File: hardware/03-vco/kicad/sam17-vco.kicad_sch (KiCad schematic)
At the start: 32 parts, among them J1 PSU +12/G/G/-12, J2 Mazo digital IDC 2x6, U10 74HC14, U11 L78L05, U12 LD1117S33TR, U13 TMP1075DGK, U14 24AA02E48, U5 AD5686RBRUZ, U6 AD5686RBRUZ, U7 AD5686RBRUZ, U8 ADR4525BRZ

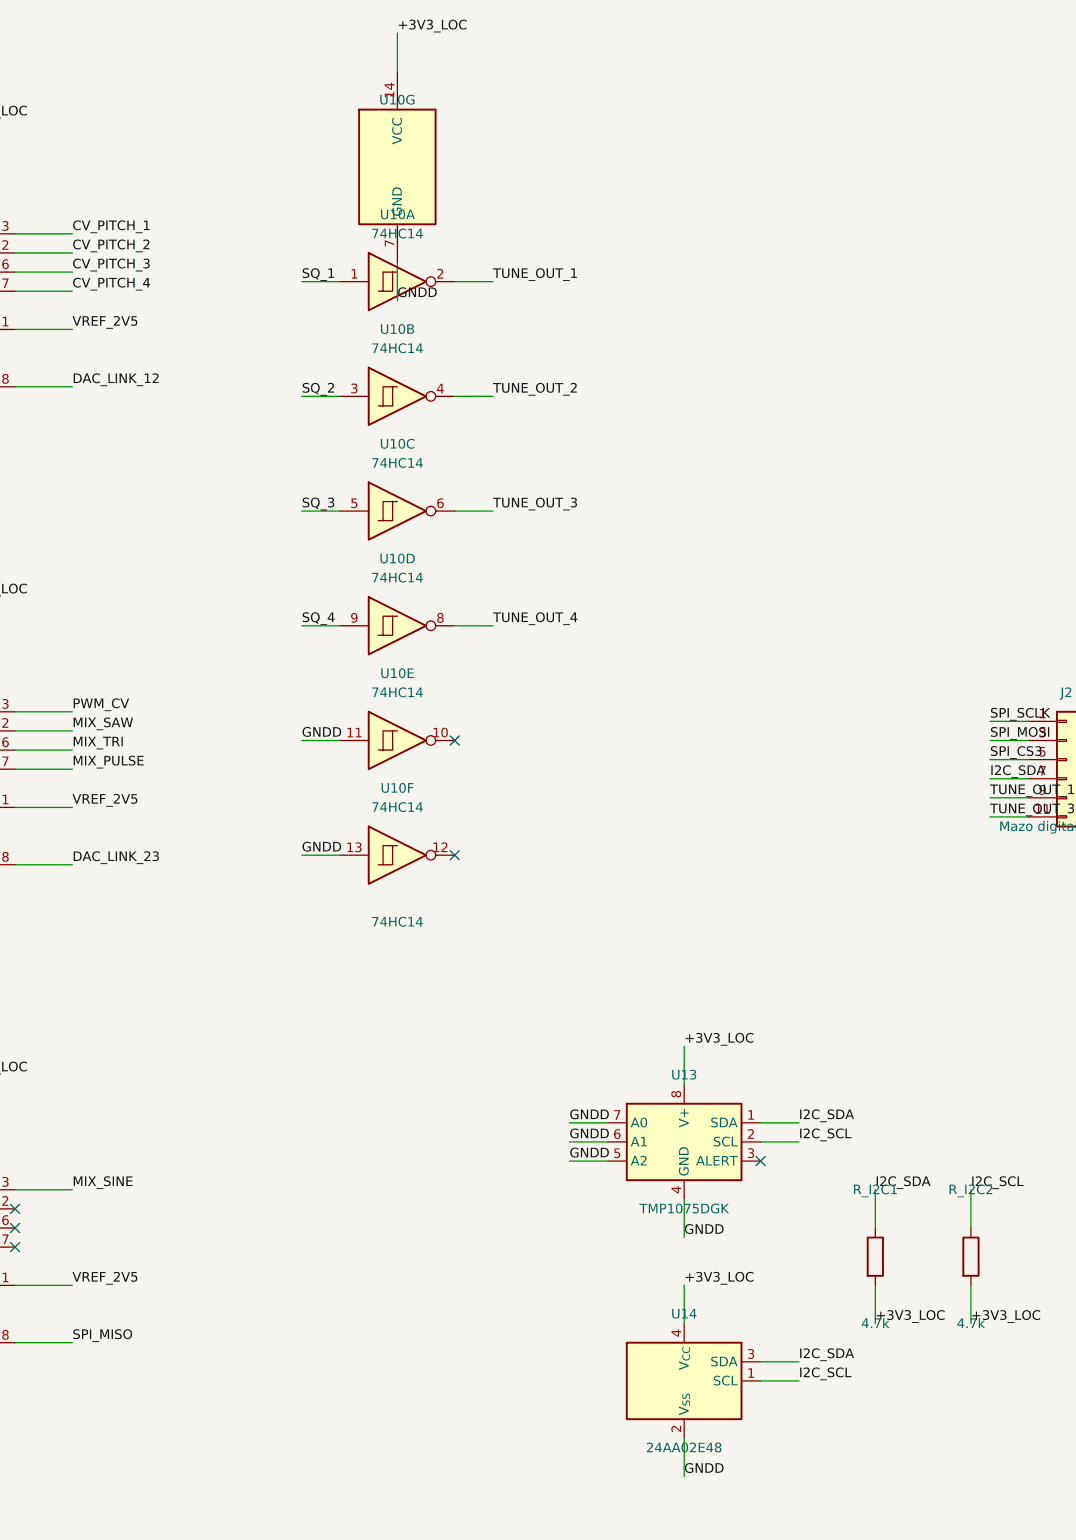
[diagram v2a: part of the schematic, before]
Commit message: Fix revision Tarea 3: desacoplos faltantes del bloque digital (C12-C20)
Finding Important de la revision: bom.csv reserva C_DEC* ("desacoplo
pegado a cada chip") como contrato y el bloque digital dejaba 6 chips sin
ninguno. Anade _desacoplo() (helper nuevo, solo usado en codigo nuevo) y 9
capacitores de 100nF:

- C12-C17 (U5-U7, en bloque_dac()): VDD y VLOGIC de cada DAC, retorno a
  GNDA -- mismo esquema que el DAC unico del modulo 2.
- C18/C19/C20 (U10/U13/U14, en bloque_hc14()/bloque_telemetria()):
  +3V3_LOC -> GNDD cada uno, su propia masa.

ERC identico violacion por violacion al de antes del fix (20: 4 errores
pin_not_driven en SQ_1..4 + 16 avisos esperados) -- los 9 capacitores
caen sobre redes que ya tenian mas miembros, sin avisos nuevos. Verificado
contra la netlist exportada, no solo contra el conteo del ERC.

RESET->+3V3_LOC y el ancho de hoja quedan sin cambio (reglados por el
controller en la misma revision).

Co-Authored-By: Claude Fable 5 <noreply@anthropic.com>
Claude-Session: https://claude.ai/code/session_01TtD4jRd4wyRdkyuChqdVe2
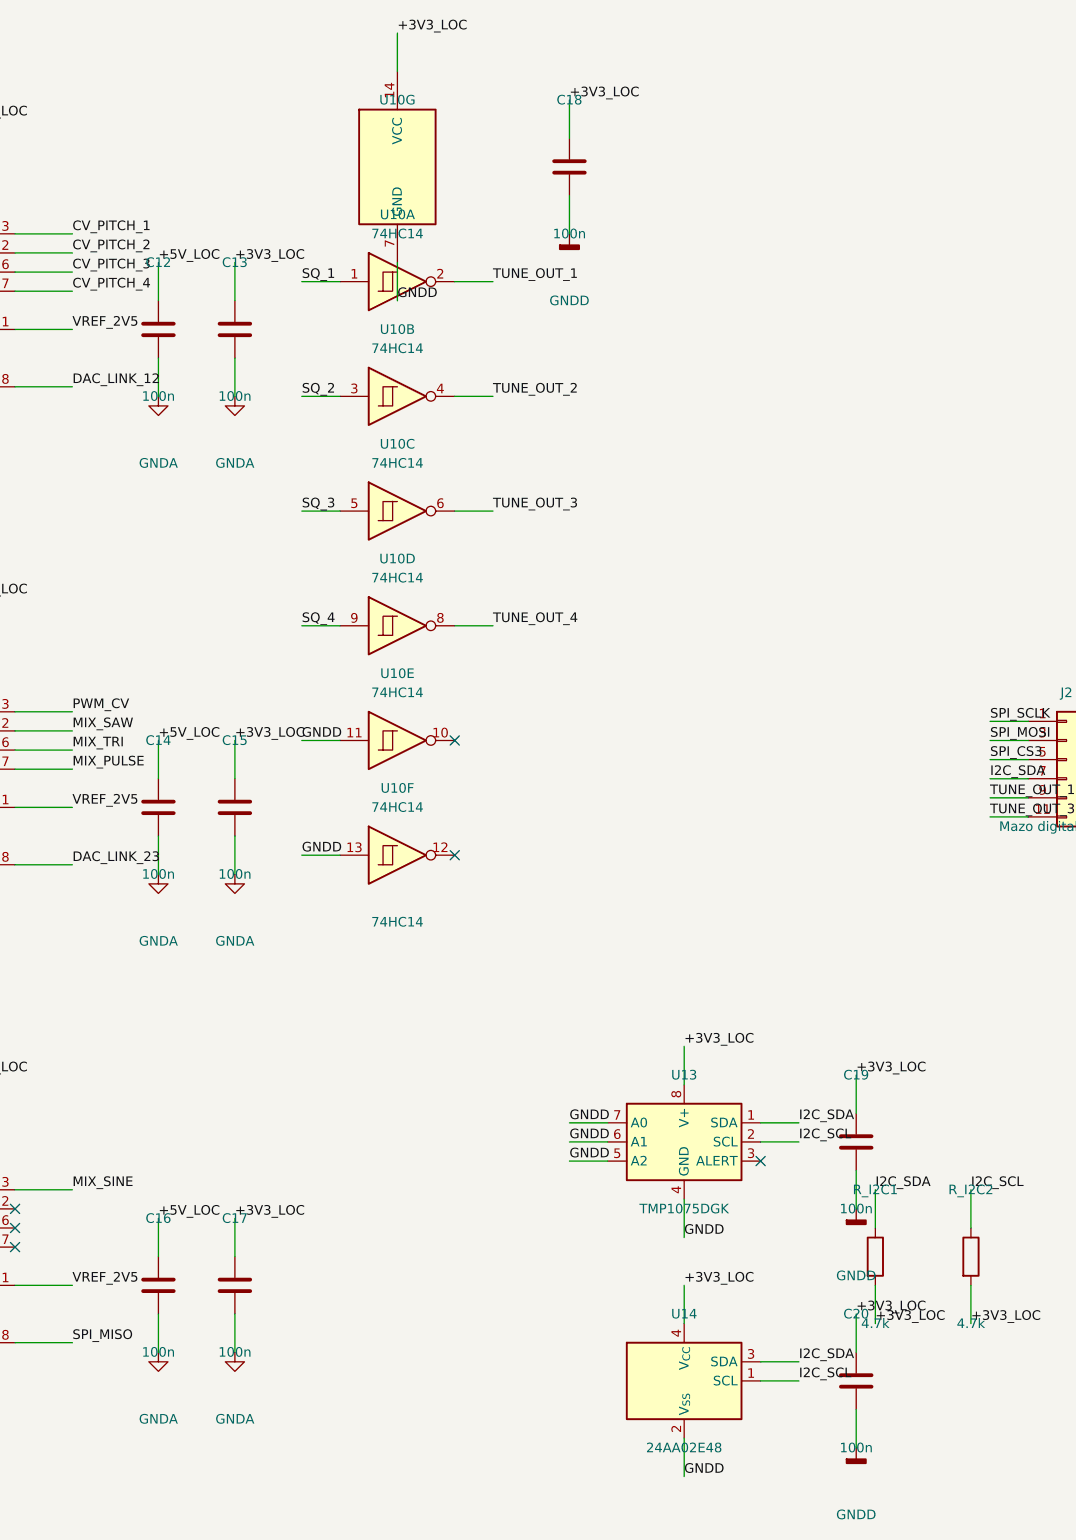
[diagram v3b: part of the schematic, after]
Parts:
- added C12, C13, C14, C15, C16, C17, C18, C19, C20: 100n, Capacitor_SMD:C_0805_2012Metric, symbol Device:C
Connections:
- net +3V3_LOC: now also C13.1, C15.1, C17.1, C18.1, C19.1, C20.1
- net +5V_LOC: now also C12.1, C14.1, C16.1
- net GNDA: now also C12.2, C13.2, C14.2, C15.2, C16.2, C17.2
- net GNDD: now also C18.2, C19.2, C20.2

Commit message: Modulo 3 VCO: dibuja las 4 voces (SSI2130 x4 + I/V + jacks), ERC a 0 errores
dibujar_voz(n, origen) llamada 4 veces: cablea los 32 pines de cada
SSI2130 (redes reales del DAC/mezclador + nodos internos para la red del
seno, EXPO FREQ, TCAP y BW COMP), el I/V compartido (unidad n de U9,
TL074, virtual a masa + R_IV 10k hasta VOICE_OUT_n) y los jacks J_CV/J_OUT
por voz. El pin 33 (EP) se salta del bucle a proposito: es no_connect de
fabrica y ponerle la cruz produce "no_connect_dangling" (mismo caso que
el pin 5 del EEPROM en la Tarea 3).

Corrige un error del brief contra el datasheet: la Figure 1 (verificada
en imagen renderizada a 400 DPI) y el texto de la pagina 6 atan PWM- (31)
al triangulo y PWM+ (32) al control de ancho de pulso -- al reves de como
traia la tabla SSI2130_CONEXION del brief.

Cierra los 4 errores pin_not_driven de SQ_1..4 y los 8 avisos de
etiqueta huerfana (SQ_1..4, PWM_CV/MIX_*, MIXO_1..4) que las Tareas 1-3
dejaron pendientes a proposito. ERC final: 0 errores, 3 warnings
pin_to_pin en VREF_2V5 (permanentes, ya documentados por la Tarea 3, sin
relacion con esta tarea).

Co-Authored-By: Claude Fable 5 <noreply@anthropic.com>
Claude-Session: https://claude.ai/code/session_01TtD4jRd4wyRdkyuChqdVe2
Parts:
- added C21, C22, C23, C24: 100n, Capacitor_SMD:C_0805_2012Metric, symbol Device:C
- added C_AC1A, C_AC1B, C_AC2A, C_AC2B, C_AC3A, C_AC3B, C_AC4A, C_AC4B: 10u, Capacitor_SMD:C_0805_2012Metric, symbol Device:C
- added C_BW1, C_BW2, C_BW3, C_BW4: 10n, Capacitor_SMD:C_0805_2012Metric, symbol Device:C
- added C_TCAP1, C_TCAP2, C_TCAP3, C_TCAP4: 3.9n C0G, Capacitor_SMD:C_0805_2012Metric, symbol Device:C
- added J_CV1, J_CV2, J_CV3, J_CV4, J_OUT1, J_OUT2, J_OUT3, J_OUT4: WQP-PJ398SM, Connector_Audio:Jack_3.5mm_QingPu_WQP-PJ398SM_Vertical_CircularHoles, symbol Connector_Audio:AudioJack2_SwitchT
- added R_BW1, R_BW2, R_BW3, R_BW4: 270R, Resistor_SMD:R_0805_2012Metric, symbol Device:R
- added R_CVIN1, R_CVIN2, R_CVIN3, R_CVIN4, R_MIX1A, R_MIX1B, R_MIX1C, R_MIX1D, R_MIX2A, R_MIX2B, R_MIX2C, R_MIX2D, R_MIX3A, R_MIX3B, R_MIX3C, R_MIX3D, R_MIX4A, R_MIX4B, R_MIX4C, R_MIX4D: 49.9k, Resistor_SMD:R_0805_2012Metric, symbol Device:R
- added R_IV1, R_IV2, R_IV3, R_IV4: 10k, Resistor_SMD:R_0805_2012Metric, symbol Device:R
- added R_PITCH1, R_PITCH2, R_PITCH3, R_PITCH4: 16.5k, Resistor_SMD:R_0805_2012Metric, symbol Device:R
- added R_SCALE1, R_SCALE2, R_SCALE3, R_SCALE4: 26.7k, Resistor_SMD:R_0805_2012Metric, symbol Device:R
- added R_SIN402_1, R_SIN402_2, R_SIN402_3, R_SIN402_4: 4.02k, Resistor_SMD:R_0805_2012Metric, symbol Device:R
- added R_SIN475A_1, R_SIN475A_2, R_SIN475A_3, R_SIN475A_4, R_SIN475B_1, R_SIN475B_2, R_SIN475B_3, R_SIN475B_4: 4.75k, Resistor_SMD:R_0805_2012Metric, symbol Device:R
- added R_SQ1, R_SQ2, R_SQ3, R_SQ4: 20k, Resistor_SMD:R_0805_2012Metric, symbol Device:R
- added U1, U2, U3, U4: SSI2130, Package_DFN_QFN:QFN-32-1EP_4x4mm_P0.4mm_EP2.65x2.65mm, symbol sam17:SSI2130
- added U9: TL074H, Package_SO:SOIC-14_3.9x8.7mm_P1.27mm, symbol Amplifier_Operational:TL074
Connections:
- net +12V: now also U9.4 (V+)
- net +3V3_LOC: now also R_SQ1.2, R_SQ2.2, R_SQ3.2, R_SQ4.2
- net +5V_LOC: now also C21.1, C22.1, C23.1, C24.1, U1.18 (TIME_REV), U1.27 (V+), U2.18 (TIME_REV), U2.27 (V+), U3.18 (TIME_REV), U3.27 (V+), U4.18 (TIME_REV), U4.27 (V+)
- net -12V: now also U1.8 (V-), U2.8 (V-), U3.8 (V-), U4.8 (V-), U9.11 (V-)
- net CV_PITCH_1: now also R_PITCH1.1
- net CV_PITCH_2: now also R_PITCH2.1
- net CV_PITCH_3: now also R_PITCH3.1
- net CV_PITCH_4: now also R_PITCH4.1
- net GNDA: now also C21.2, C22.2, C23.2, C24.2, C_BW1.2, C_BW2.2, C_BW3.2, C_BW4.2, C_TCAP1.2, C_TCAP2.2, C_TCAP3.2, C_TCAP4.2, J_CV1.S, J_CV1.TN, J_CV2.S, J_CV2.TN, J_CV3.S, J_CV3.TN, J_CV4.S, J_CV4.TN, J_OUT1.S, J_OUT2.S, J_OUT3.S, J_OUT4.S, R_SIN475A_1.2, R_SIN475A_2.2, R_SIN475A_3.2, R_SIN475A_4.2, R_SIN475B_1.2, R_SIN475B_2.2, R_SIN475B_3.2, R_SIN475B_4.2, U1.13 (MIX_AUX2), U1.15 (DGND), U1.16 (AGND), U1.17 (HARD_SYNC), U1.20 (HFT_BASE), U2.13 (MIX_AUX2), U2.15 (DGND), U2.16 (AGND), U2.17 (HARD_SYNC), U2.20 (HFT_BASE), U3.13 (MIX_AUX2), U3.15 (DGND), U3.16 (AGND), U3.17 (HARD_SYNC), U3.20 (HFT_BASE), U4.13 (MIX_AUX2), U4.15 (DGND), U4.16 (AGND), U4.17 (HARD_SYNC), U4.20 (HFT_BASE), U9.10 (+), U9.12 (+), U9.3 (+), U9.5 (+)
- net MIXO_1: now also R_IV1.1, U1.25 (MIX_OUT), U9.2 (-)
- net MIXO_2: now also R_IV2.1, U2.25 (MIX_OUT), U9.6 (-)
- net MIXO_3: now also R_IV3.1, U3.25 (MIX_OUT), U9.9 (-)
- net MIXO_4: now also R_IV4.1, U4.25 (MIX_OUT), U9.13 (-)
- net MIX_PULSE: now also R_MIX1C.1, R_MIX2C.1, R_MIX3C.1, R_MIX4C.1
- net MIX_SAW: now also R_MIX1B.1, R_MIX2B.1, R_MIX3B.1, R_MIX4B.1
- net MIX_SINE: now also R_MIX1D.1, R_MIX2D.1, R_MIX3D.1, R_MIX4D.1
- net MIX_TRI: now also R_MIX1A.1, R_MIX2A.1, R_MIX3A.1, R_MIX4A.1
- net PWM_CV: now also U1.32 (PWM+), U2.32 (PWM+), U3.32 (PWM+), U4.32 (PWM+)
- net SQ_1: now also R_SQ1.1, U1.28 (SQUARE_OUT)
- net SQ_2: now also R_SQ2.1, U2.28 (SQUARE_OUT)
- net SQ_3: now also R_SQ3.1, U3.28 (SQUARE_OUT)
- net SQ_4: now also R_SQ4.1, U4.28 (SQUARE_OUT)
- net VREF_2V5: now also R_SCALE1.1, R_SCALE2.1, R_SCALE3.1, R_SCALE4.1, U1.23 (VREF), U2.23 (VREF), U3.23 (VREF), U4.23 (VREF)
- new net CVIN_1: J_CV1.T, R_CVIN1.1
- new net CVIN_2: J_CV2.T, R_CVIN2.1
- new net CVIN_3: J_CV3.T, R_CVIN3.1
- new net CVIN_4: J_CV4.T, R_CVIN4.1
- new net N10_1: R_MIX1B.2, U1.10 (MIX_SAW)
- new net N10_2: R_MIX2B.2, U2.10 (MIX_SAW)
- new net N10_3: R_MIX3B.2, U3.10 (MIX_SAW)
- new net N10_4: R_MIX4B.2, U4.10 (MIX_SAW)
- new net N11_1: R_MIX1C.2, U1.11 (MIX_PULSE)
- new net N11_2: R_MIX2C.2, U2.11 (MIX_PULSE)
- new net N11_3: R_MIX3C.2, U3.11 (MIX_PULSE)
- new net N11_4: R_MIX4C.2, U4.11 (MIX_PULSE)
- new net N12_1: R_MIX1D.2, U1.12 (MIX_AUX1)
- new net N12_2: R_MIX2D.2, U2.12 (MIX_AUX1)
- new net N12_3: R_MIX3D.2, U3.12 (MIX_AUX1)
- new net N12_4: R_MIX4D.2, U4.12 (MIX_AUX1)
- new net N14_1: C_TCAP1.1, U1.14 (TCAP)
- new net N14_2: C_TCAP2.1, U2.14 (TCAP)
- new net N14_3: C_TCAP3.1, U3.14 (TCAP)
- new net N14_4: C_TCAP4.1, U4.14 (TCAP)
- new net N22_1: R_SCALE1.2, U1.22 (EXPO_SCALE)
- new net N22_2: R_SCALE2.2, U2.22 (EXPO_SCALE)
- new net N22_3: R_SCALE3.2, U3.22 (EXPO_SCALE)
- new net N22_4: R_SCALE4.2, U4.22 (EXPO_SCALE)
- new net N26M_1: C_BW1.1, R_BW1.2
- new net N26M_2: C_BW2.1, R_BW2.2
- new net N26M_3: C_BW3.1, R_BW3.2
- new net N26M_4: C_BW4.1, R_BW4.2
- new net N26_1: R_BW1.1, U1.26 (BW_COMP)
- new net N26_2: R_BW2.1, U2.26 (BW_COMP)
- new net N26_3: R_BW3.1, U3.26 (BW_COMP)
- new net N26_4: R_BW4.1, U4.26 (BW_COMP)
- new net N2M_1: C_AC1A.2, R_SIN402_1.1
- new net N2M_2: C_AC2A.2, R_SIN402_2.1
- new net N2M_3: C_AC3A.2, R_SIN402_3.1
- new net N2M_4: C_AC4A.2, R_SIN402_4.1
- new net N2_1: R_SIN402_1.2, R_SIN475A_1.1, U1.2 (SINE_IN+)
- new net N2_2: R_SIN402_2.2, R_SIN475A_2.1, U2.2 (SINE_IN+)
- new net N2_3: R_SIN402_3.2, R_SIN475A_3.1, U3.2 (SINE_IN+)
- new net N2_4: R_SIN402_4.2, R_SIN475A_4.1, U4.2 (SINE_IN+)
- new net N3_1: R_SIN475B_1.1, U1.3 (SINE_IN-)
- new net N3_2: R_SIN475B_2.1, U2.3 (SINE_IN-)
- new net N3_3: R_SIN475B_3.1, U3.3 (SINE_IN-)
- new net N3_4: R_SIN475B_4.1, U4.3 (SINE_IN-)
- new net N4_1: C_AC1B.2, U1.4 (AUX1_IN)
- new net N4_2: C_AC2B.2, U2.4 (AUX1_IN)
- new net N4_3: C_AC3B.2, U3.4 (AUX1_IN)
- new net N4_4: C_AC4B.2, U4.4 (AUX1_IN)
- new net N7_1: R_CVIN1.2, R_PITCH1.2, U1.7 (EXPO_FREQ)
- new net N7_2: R_CVIN2.2, R_PITCH2.2, U2.7 (EXPO_FREQ)
- new net N7_3: R_CVIN3.2, R_PITCH3.2, U3.7 (EXPO_FREQ)
- new net N7_4: R_CVIN4.2, R_PITCH4.2, U4.7 (EXPO_FREQ)
- new net N9_1: R_MIX1A.2, U1.9 (MIX_TRI)
- new net N9_2: R_MIX2A.2, U2.9 (MIX_TRI)
- new net N9_3: R_MIX3A.2, U3.9 (MIX_TRI)
- new net N9_4: R_MIX4A.2, U4.9 (MIX_TRI)
- new net SINEO_1: C_AC1B.1, U1.24 (SINE_OUT)
- new net SINEO_2: C_AC2B.1, U2.24 (SINE_OUT)
- new net SINEO_3: C_AC3B.1, U3.24 (SINE_OUT)
- new net SINEO_4: C_AC4B.1, U4.24 (SINE_OUT)
- new net TRI_1: C_AC1A.1, U1.1 (TRI_OUT), U1.31 (PWM-)
- new net TRI_2: C_AC2A.1, U2.1 (TRI_OUT), U2.31 (PWM-)
- new net TRI_3: C_AC3A.1, U3.1 (TRI_OUT), U3.31 (PWM-)
- new net TRI_4: C_AC4A.1, U4.1 (TRI_OUT), U4.31 (PWM-)
- new net VOICE_OUT_1: J_OUT1.T, R_IV1.2, U9.1
- new net VOICE_OUT_2: J_OUT2.T, R_IV2.2, U9.7
- new net VOICE_OUT_3: J_OUT3.T, R_IV3.2, U9.8
- new net VOICE_OUT_4: J_OUT4.T, R_IV4.2, U9.14
- no-connect marks 11 -> 39

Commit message: Modulo 3 VCO: fix de revision -- LIN FREQ, MIX AUX2, desacoplo V-/bulk, ERC 0/0
Corrige 3 findings reales de la revision contra el datasheet (misma clase
de error que el PWM ya cazado: manda la Figure 1 + el texto de aplicacion,
no el borrador del brief):

- LIN FREQ (pin 21) ya no queda NC: sin ~5uA ahi el oscilador SE PARA (ds
  pag.5 y pag.9, "0 current in equals 0 frequency out"). R_LIN{n} 499k
  desde VREF_2V5 en cada voz.
- MIX AUX2 (pin 13) deja de ir a masa directa: el datasheet (pag.8) lo
  prohibe explicitamente para canales de mezcla sin usar ("Do not connect
  control inputs directly to ground"). Pasa a NC, igual que su otro
  extremo (AUX2 IN, pin 5).
- Desacoplo de 100nF en V- (pin 8) pegado a cada SSI2130, y bulk de 10uF
  en +12V y -12V tal como entran por J1 -- el datasheet (pag.6) pide
  decoupling y bulk en AMBAS alimentaciones, no solo en V+/+5V_LOC.

Riders aprobados en el mismo round:
- Retipa el pin VREF del AD5686RBRUZ de bidirectional a input en el
  sam17.kicad_sym LOCAL de este modulo (no el del modulo 2: alli el pin
  si es salida). En esta placa la referencia interna del DAC se apaga por
  firmware, asi que el pin es solo entrada -- mata los 3 avisos
  pin_to_pin que quedaban desde la Tarea 3.
- Hoja a (paper "User" 500 1000) para que las 4 voces quepan en el area
  ploteable.
- Assert de cobertura: _redes_ssi2130() se valida contra los pines reales
  del simbolo (menos EP) para que una clave borrada tumbe el build en vez
  de colarse como una cruz NC silenciosa.

ERC final: 0 errores, 0 avisos, exit code 0. bom.csv actualizado (fila
R_LIN nueva, C_DEC*/C_BULK* reconciliados con las piezas reales
colocadas).

Co-Authored-By: Claude Fable 5 <noreply@anthropic.com>
Claude-Session: https://claude.ai/code/session_01TtD4jRd4wyRdkyuChqdVe2
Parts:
- added C25, C26: 10u, Capacitor_SMD:C_0805_2012Metric, symbol Device:C
- added C27, C28, C29, C30: 100n, Capacitor_SMD:C_0805_2012Metric, symbol Device:C
- added R_LIN1, R_LIN2, R_LIN3, R_LIN4: 499k, Resistor_SMD:R_0805_2012Metric, symbol Device:R
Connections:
- net +12V: now also C25.1
- net -12V: now also C26.1, C27.1, C28.1, C29.1, C30.1
- net GNDA: now also C25.2, C26.2, C27.2, C28.2, C29.2, C30.2; no longer U1.13 (MIX_AUX2), U2.13 (MIX_AUX2), U3.13 (MIX_AUX2), U4.13 (MIX_AUX2)
- net VREF_2V5: now also R_LIN1.1, R_LIN2.1, R_LIN3.1, R_LIN4.1
- net N21_3: now reaches U3.21 (LIN_FREQ)
- net N21_3: now also R_LIN3.2
- net N21_1: now reaches U1.21 (LIN_FREQ)
- net N21_1: now also R_LIN1.2
- net N21_4: now reaches U4.21 (LIN_FREQ)
- net N21_4: now also R_LIN4.2
- net N21_2: now reaches U2.21 (LIN_FREQ)
- net N21_2: now also R_LIN2.2

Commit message: El BOM del modulo 3 deja de ser una lista de deseos: 23 de 26 con stock real
Verificado pieza por pieza contra la libreria de ensamblaje de JLCPCB el
2026-08-17, no contra memoria. Cada linea lleva su MPN, su stock y la fecha.

El matcher automatico de JLC proponia cinco cosas que habrian pasado calladas:
3.9nF en X7R donde el datasheet exige C0G (el tempo derivaria con la
temperatura y el modulo desafinaria solo), 220k donde va un 20k, 16.5k y 499k
en huella 0402 sobre pads de 0805, y ningun match para un 270R que si existe.
Ninguna de las cinco rompe un test; todas rompen la placa.

R_LIN pasa de 499k a 510k. El datasheet pide 499k y ese valor no existe en
0805 en el catalogo de JLC -- ni stock ni pre-order --, y la placa no se
monta a mano. El cambio se sostiene en la pag.4: la corriente de LIN FREQ
"sets the linear scale of the exponential converter's output", o sea escala
la curva de forma multiplicativa, asi que un desvio NO toca el tracking de
1V/oct. 510k da 4.902uA contra 5.010uA: -38 cents identicos en las cuatro
voces, y hacia el grave, que gana margen en vez de gastarlo. El 470k tambien
habia y se descarto: +104 cents.

Quedan tres lineas abiertas, todas con mecanismo confirmado:
- R_PITCH (16.5k) y R_SIN402 (4.02k): stock 0 en 0805 pero si hay pre-order,
  ~$8.70 y ~$8.60 el lote minimo.
- SSI2130: hay dos entradas en JLC y solo una sirve. C2886621 tiene MOQ 75 e
  es inservible; C42420746 (Sound Semiconductor) admite minimo 1 a ~$24.80.

ERC 0/0, check_netlist 152 redes, check_bom 136 componentes, los cuatro
presupuestos verdes. La placa no cambia: misma huella, mismos gerbers.

Co-Authored-By: Claude Fable 5 <noreply@anthropic.com>
Claude-Session: https://claude.ai/code/session_01TtD4jRd4wyRdkyuChqdVe2
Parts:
- R_LIN1, R_LIN2, R_LIN3, R_LIN4: value 499k -> 510k
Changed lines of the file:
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@@
 			)
 		)
-		(property "Value" "499k"
+		(property "Value" "510k"
 			(at 177.79999999999998 308.61 0)
 			(show_name no)
@@
 			)
 		)
-		(property "Value" "499k"
+		(property "Value" "510k"
 			(at 177.79999999999998 524.51 0)
 			(show_name no)
@@
 			)
 		)
-		(property "Value" "499k"
+		(property "Value" "510k"
 			(at 177.79999999999998 740.41 0)
 			(show_name no)
@@
 			)
 		)
-		(property "Value" "499k"
+		(property "Value" "510k"
 			(at 177.79999999999998 956.31 0)
 			(show_name no)

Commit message: Revierte el 510k: el 499k del datasheet SI esta en stock, lo lei mal
El commit anterior cambio R_LIN de 499k a 510k con el argumento de que el
499k no existia en 0805 en el catalogo de JLC. Es falso: C17721 (UNI-ROYAL
0805W8F4993T5E) tiene 115981 unidades. Lo mismo con las otras dos lineas que
di por perdidas -- 16.5k es C35929 (4749) y 4.02k es C17663 (31954).

La causa: capture las tres paginas del buscador a medio cargar. La seccion
"In stock Parts" todavia no habia pintado y la pestaña "Consign Parts" era
lo unico visible, asi que lei "no hay stock" donde decia "aun no cargo".
El razonamiento sobre el datasheet era correcto y sigue anotado por si algun
dia hace falta mover el valor de verdad; lo que estaba mal era la premisa.

El diseño vuelve exacto a su estado previo: netlist semanticamente identica
a 19f79df^ (solo cambian UUIDs y fecha, que el generador re-crea por corrida).

Con eso el BOM queda CERRADO: 111 de 111 piezas con codigo LCSC verificado.

Se añaden ademas los dos generadores que faltaban para poder pedir:
- bom_jlc.py: fusiona las filas que comparten codigo (los 10uF salen en dos
  filas y los 49.9k en dos), porque JLC marca duplicado el mismo part number
  en dos renglones. Falla en vez de escribir si algo quedo sin codigo.
- cpl_jlc.py: el pos.csv crudo NO sirve, falla con "Failed processing the CPL
  file" -- JLC espera Designator,Mid X,Mid Y,Layer,Rotation con Layer
  capitalizado y 2 decimales. Cruza BOM y posiciones en los dos sentidos.

ERC 0/0, check_netlist 152 redes, check_bom 136 componentes, los cuatro
presupuestos verdes.

Co-Authored-By: Claude Fable 5 <noreply@anthropic.com>
Claude-Session: https://claude.ai/code/session_01TtD4jRd4wyRdkyuChqdVe2
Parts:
- R_LIN1, R_LIN2, R_LIN3, R_LIN4: value 510k -> 499k
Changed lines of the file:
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@@
 			)
 		)
-		(property "Value" "510k"
+		(property "Value" "499k"
 			(at 177.79999999999998 308.61 0)
 			(show_name no)
@@
 			)
 		)
-		(property "Value" "510k"
+		(property "Value" "499k"
 			(at 177.79999999999998 524.51 0)
 			(show_name no)
@@
 			)
 		)
-		(property "Value" "510k"
+		(property "Value" "499k"
 			(at 177.79999999999998 740.41 0)
 			(show_name no)
@@
 			)
 		)
-		(property "Value" "510k"
+		(property "Value" "499k"
 			(at 177.79999999999998 956.31 0)
 			(show_name no)
